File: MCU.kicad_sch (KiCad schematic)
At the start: 16 parts, among them J1 USB_C_Receptacle, J3 Conn_01x06, SW3 SW_Push, SW4 SW_Push, SW5 SW_Push, SW6 SW_Push, SW7 SW_Push, U11 ESDR0502NMUTBG, U3 NORA-B106-00B, U8 FAN5622SX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

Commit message: WIP changes
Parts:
- removed J1: USB_C_Receptacle, Connector_USB:USB_C_Receptacle_Amphenol_12401548E4-2A, symbol Connector:USB_C_Receptacle
- added J5: USB_C_Receptacle_USB2.0_16P, Connector_USB:USB_C_Receptacle_GCT_USB4105-xx-A_16P_TopMnt_Horizontal, symbol Connector:USB_C_Receptacle_USB2.0_16P
- SW3: footprint SKRPACE:SW_SKRPACE010_AAL -> Resistor_SMD:R_0805_2012Metric
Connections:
- net CC1: now also J5.A5 (CC1)
- net CC2: now also J5.B5 (CC2)
- net GND: now also J5.A1 (GND), J5.A12 (GND), J5.B1 (GND), J5.B12 (GND), J5.SH (SHIELD)
- net USBC_D+: now also J5.A6 (D+), J5.B6 (D+)
- net USBC_D-: now also J5.A7 (D-), J5.B7 (D-)
- net USB_RST: now also J5.A8 (SBU1), J5.B8 (SBU2)
- net VBUS_IN: now also J5.A4 (VBUS), J5.A9 (VBUS), J5.B4 (VBUS), J5.B9 (VBUS)
- no-connect marks 25 -> 17
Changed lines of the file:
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@@
 	)
 	(junction
-		(at 172.72 157.48)
+		(at 25.4 100.33)
 		(diameter 0)
 		(color 0 0 0 0)
 	)
 	(junction
-		(at 40.64 118.11)
+		(at 172.72 157.48)
 		(diameter 0)
 		(color 0 0 0 0)
@@
 	)
 	(junction
-		(at 25.4 128.27)
+		(at 40.64 90.17)
 		(diameter 0)
 		(color 0 0 0 0)
@@
 	)
 	(no_connect
-		(at 40.64 97.79)
-	)
-	(no_connect
 		(at 172.72 53.34)
 	)
@@
 	)
 	(no_connect
-		(at 40.64 95.25)
-	)
-	(no_connect
 		(at 116.84 60.96)
 	)
@@
 	)
 	(no_connect
-		(at 40.64 105.41)
-	)
-	(no_connect
 		(at 172.72 60.96)
 	)
@@
 	)
 	(no_connect
-		(at 40.64 102.87)
-	)
-	(no_connect
 		(at 172.72 45.72)
 	)
 	(no_connect
-		(at 40.64 110.49)
-	)
-	(no_connect
 		(at 116.84 91.44)
 	)
@@
 		(at 172.72 76.2)
 	)
-	(no_connect
-		(at 40.64 113.03)
-	)
-	(no_connect
-		(at 40.64 90.17)
-	)
-	(no_connect
-		(at 40.64 87.63)
-	)
 	(wire
 		(pts
@@
 	(wire
 		(pts
-			(xy 40.64 118.11) (xy 50.8 118.11)
+			(xy 40.64 90.17) (xy 50.8 90.17)
 		)
 		(stroke
@@
 	(wire
 		(pts
-			(xy 40.64 118.11) (xy 40.64 120.65)
+			(xy 40.64 90.17) (xy 40.64 92.71)
 		)
 		(stroke
@@
 	(wire
 		(pts
-			(xy 25.4 128.27) (xy 17.78 128.27)
+			(xy 25.4 100.33) (xy 17.78 100.33)
 		)
 		(stroke
@@
 	)
 	(label "USB_RST"
-		(at 50.8 118.11 180)
+		(at 50.8 90.17 180)
 		(effects
 			(font
@@
 			)
 		)
-		(property "Footprint" "SKRPACE:SW_SKRPACE010_AAL"
+		(property "Footprint" "Resistor_SMD:R_0805_2012Metric"
 			(at 104.14 25.4 0)
 			(hide yes)
@@
 	)
 	(symbol
+		(lib_id "Connector:USB_C_Receptacle_USB2.0_16P")
+		(at 25.4 77.47 0)
+		(unit 1)
+		(body_style 1)
+		(exclude_from_sim no)
+		(in_bom yes)
+		(on_board yes)
+		(in_pos_files yes)
+		(dnp no)
+		(fields_autoplaced yes)
+		(property "Reference" "J5"
+			(at 25.4 55.5455 0)
+			(show_name no)
+			(do_not_autoplace no)
+			(effects
+				(font
+					(size 1.27 1.27)
+				)
+			)
+		)
+		(property "Value" "USB_C_Receptacle_USB2.0_16P"
+			(at 25.4 57.9698 0)
+			(show_name no)
+			(do_not_autoplace no)
+			(effects
+				(font
+					(size 1.27 1.27)
+				)
+			)
+		)
+		(property "Footprint" "Connector_USB:USB_C_Receptacle_GCT_USB4105-xx-A_16P_TopMnt_Horizontal"
+			(at 29.21 77.47 0)
+			(hide yes)
+			(show_name no)
+			(do_not_autoplace no)
+			(effects
+				(font
+					(size 1.27 1.27)
+				)
+			)
+		)
+		(property "Datasheet" "https://www.usb.org/sites/default/files/documents/usb_type-c.zip"
+			(at 29.21 77.47 0)
+			(hide yes)
+			(show_name no)
+			(do_not_autoplace no)
+			(effects
+				(font
+					(size 1.27 1.27)
+				)
+			)
+		)
+		(property "Description" "USB 2.0-only 16P Type-C Receptacle connector"
+			(at 25.4 77.47 0)
+			(hide yes)
+			(show_name no)
+			(do_not_autoplace no)
+			(effects
+				(font
+					(size 1.27 1.27)
+				)
+			)
+		)
+		(pin "A9"
+		)
+		(pin "A7"
+		)
+		(pin "A8"
+		)
+		(pin "A5"
+		)
+		(pin "B5"
+		)
+		(pin "B12"
+		)
+		(pin "B4"
+		)
+		(pin "A1"
+		)
+		(pin "SH"
+		)
+		(pin "A4"
+		)
+		(pin "B7"
+		)
+		(pin "B6"
+		)
+		(pin "B9"
+		)
+		(pin "A6"
+		)
+		(pin "A12"
+		)
+		(pin "B1"
+		)
+		(pin "B8"
+		)
+		(instances
+			(project "Smart_Watch"
+				(path "/69095a4d-0a57-4fa3-aecb-1cfd89eedc11/bed567dd-6d09-419a-b99a-3e57c9439bd4/30bd5bb3-3a33-4afa-baf2-7512abedf580"
+					(reference "J5")
+					(unit 1)
+				)
+			)
+		)
+	)
+	(symbol
 		(lib_id "power:+3V0")
 		(at 241.3 66.04 0)
@@
 	(symbol
 		(lib_id "power:GND")
-		(at 25.4 128.27 0)
+		(at 25.4 100.33 0)
 		(unit 1)
 		(body_style 1)
@@
 		(fields_autoplaced yes)
 		(property "Reference" "#PWR065"
-			(at 25.4 134.62 0)
+			(at 25.4 106.68 0)
 			(hide yes)
 			(show_name no)
@@
 		)
 		(property "Value" "GND"
-			(at 25.4 132.4031 0)
+			(at 25.4 104.4631 0)
 			(show_name no)
 			(do_not_autoplace no)
@@
 		)
 		(property "Footprint" ""
-			(at 25.4 128.27 0)
+			(at 25.4 100.33 0)
 			(hide yes)
 			(show_name no)
@@
 		)
 		(property "Datasheet" ""
-			(at 25.4 128.27 0)
+			(at 25.4 100.33 0)
 			(hide yes)
 			(show_name no)
@@
 		)
 		(property "Description" "Power symbol creates a global label with name \"GND\" , ground"
-			(at 25.4 128.27 0)
+			(at 25.4 100.33 0)
 			(hide yes)
 			(show_name no)
@@
 				)
 			)
-		)
-	)
-	(symbol
-		(lib_id "Connector:USB_C_Receptacle")
-		(at 25.4 87.63 0)
-		(unit 1)
-		(body_style 1)
-		(exclude_from_sim no)
-		(in_bom yes)
-		(on_board yes)
-		(in_pos_files yes)
-		(dnp no)
-		(fields_autoplaced yes)
-		(property "Reference" "J1"
-			(at 25.4 55.5455 0)
-			(show_name no)
-			(do_not_autoplace no)
-			(effects
-				(font
-					(size 1.27 1.27)
-				)
-			)
-		)
-		(property "Value" "USB_C_Receptacle"
-			(at 25.4 57.9698 0)
-			(show_name no)
-			(do_not_autoplace no)
-			(effects
-				(font
-					(size 1.27 1.27)
-				)
-			)
-		)
-		(property "Footprint" "Connector_USB:USB_C_Receptacle_Amphenol_12401548E4-2A"
-			(at 29.21 87.63 0)
-			(hide yes)
-			(show_name no)
-			(do_not_autoplace no)
-			(effects
-				(font
-					(size 1.27 1.27)
-				)
-			)
-		)
-		(property "Datasheet" "https://www.usb.org/sites/default/files/documents/usb_type-c.zip"
-			(at 29.21 87.63 0)
-			(hide yes)
-			(show_name no)
-			(do_not_autoplace no)
-			(effects
-				(font
-					(size 1.27 1.27)
-				)
-			)
-		)
-		(property "Description" "USB Full-Featured Type-C Receptacle connector"
-			(at 25.4 87.63 0)
-			(hide yes)
-			(show_name no)
-			(do_not_autoplace no)
-			(effects
-				(font
-					(size 1.27 1.27)
-				)
-			)
-		)
-		(pin "B12"
-		)
-		(pin "A9"
-		)
-		(pin "B9"
-		)
-		(pin "S1"
-		)
-		(pin "A7"
-		)
-		(pin "A12"
-		)
-		(pin "A1"
-		)
-		(pin "B1"
-		)
-		(pin "A4"
-		)
-		(pin "B4"
-		)
-		(pin "B5"
-		)
-		(pin "A5"
-		)
-		(pin "A11"
-		)
-		(pin "B6"
-		)
-		(pin "B11"
-		)
-		(pin "B2"
-		)
-		(pin "A6"
-		)
-		(pin "A3"
-		)
-		(pin "A2"
-		)
-		(pin "B3"
-		)
-		(pin "A10"
-		)
-		(pin "A8"
-		)
-		(pin "B10"
-		)
-		(pin "B8"
-		)
-		(pin "B7"
-		)
-		(instances
-			(project "Smart_Watch"
-				(path "/69095a4d-0a57-4fa3-aecb-1cfd89eedc11/bed567dd-6d09-419a-b99a-3e57c9439bd4/30bd5bb3-3a33-4afa-baf2-7512abedf580"
-					(reference "J1")
-					(unit 1)
-					(variant
-						(name "No Trans")
-					)
-					(variant
-						(name "W Trans")
-					)
-				)
-			)

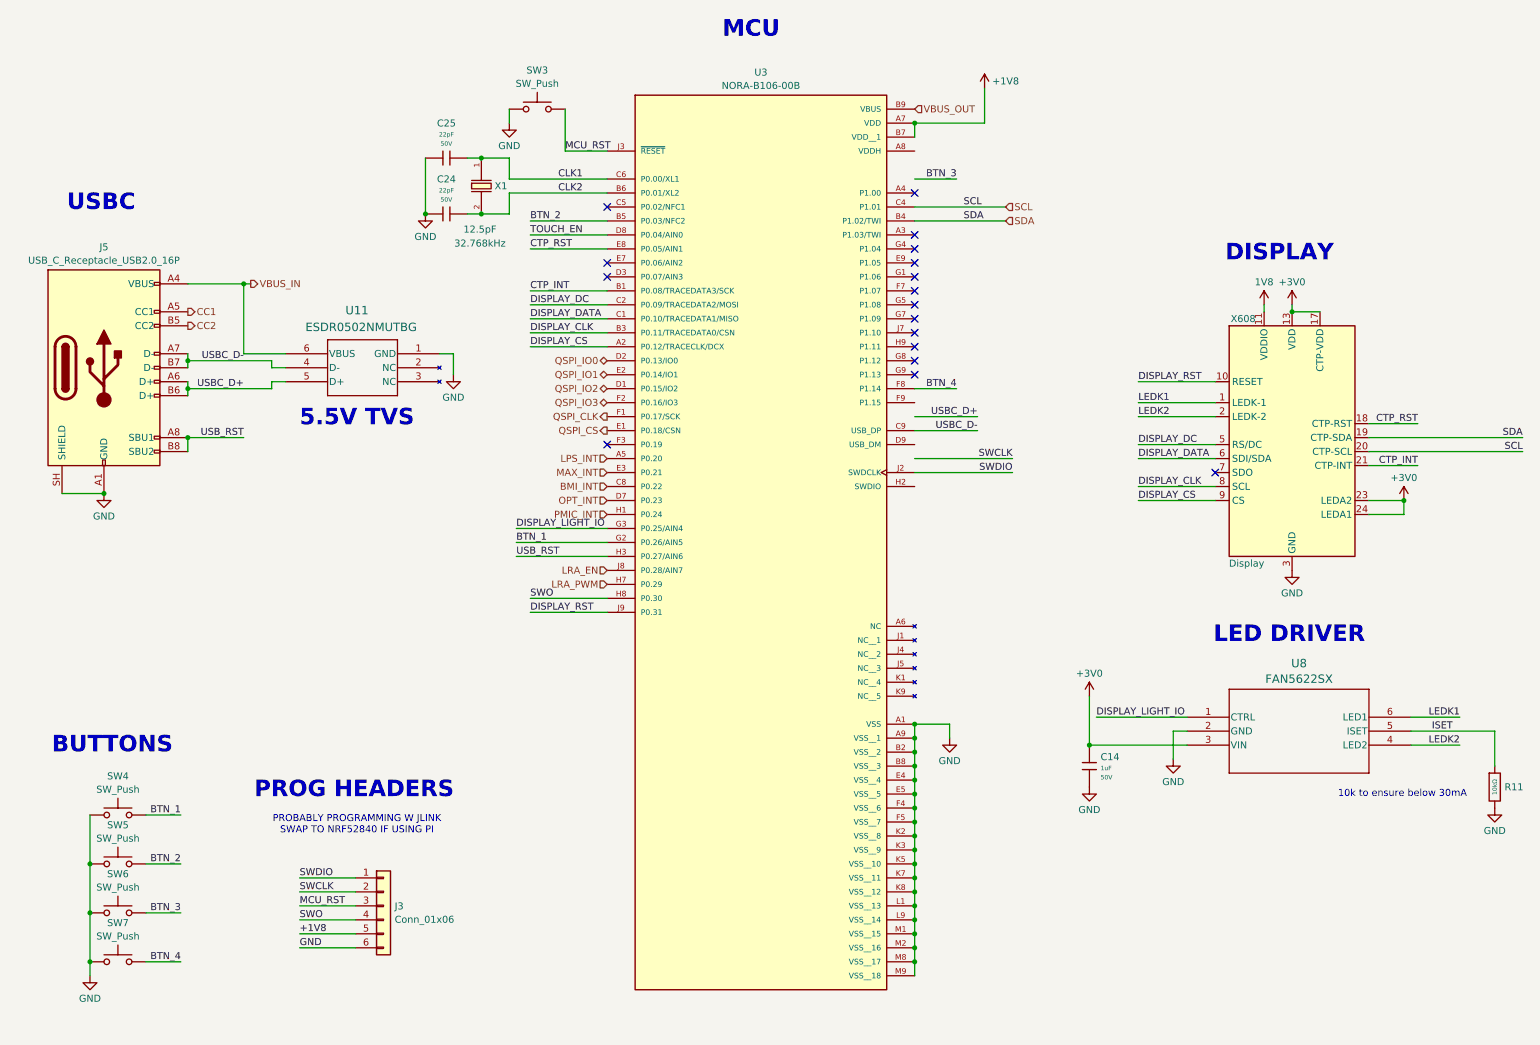
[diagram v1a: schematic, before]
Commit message: Update the last components and change a couple
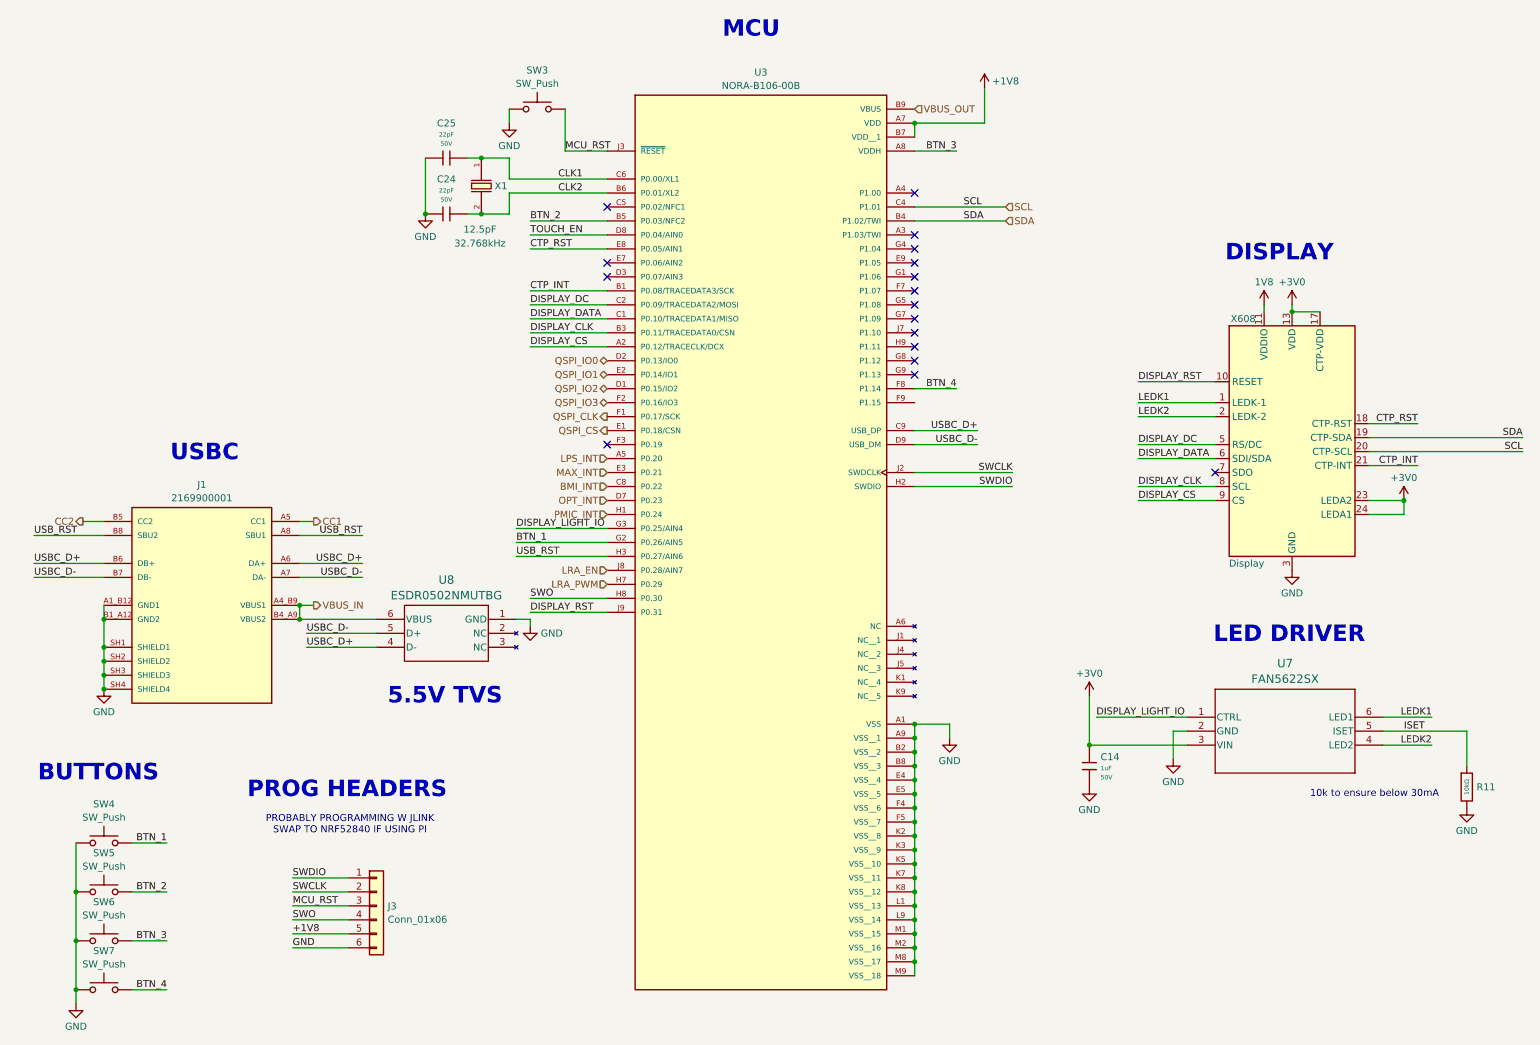
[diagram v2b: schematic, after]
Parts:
- removed J5: USB_C_Receptacle_USB2.0_16P, Connector_USB:USB_C_Receptacle_GCT_USB4105-xx-A_16P_TopMnt_Horizontal, symbol Connector:USB_C_Receptacle_USB2.0_16P
- removed U11: ESDR0502NMUTBG, ESD:UDFN6_517AA_ONS, symbol 2026-04-16_01-33-00:ESDR0502NMUTBG
- removed U8: FAN5622SX, FAN:SSOT6_3X1P7_ONS, symbol 2026-04-09_01-28-48:FAN5622SX
- added J1: 2169900001, Smart_Watch:MOLEX_2169900001, symbol Smart_Watch:2169900001
- added U7: FAN5622SX, Smart_Watch:SSOT6_3X1P7_ONS-L, symbol Smart_Watch:FAN5622SX
- added U8: ESDR0502NMUTBG, Smart_Watch:UDFN6_517AA_ONS-L, symbol Smart_Watch:ESDR0502NMUTBG
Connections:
- net +3V0: now also U7.3 (VIN)
- net BTN_3: now also U3.A8 (VDDH)
- net CC1: now also J1.A5 (CC1)
- net CC2: now also J1.B5 (CC2)
- net DISPLAY_LIGHT_IO: now also U7.1 (CTRL)
- net GND: now also J1.A1_B12 (GND1), J1.B1_A12 (GND2), J1.SH1 (SHIELD1), J1.SH2 (SHIELD2), J1.SH3 (SHIELD3), J1.SH4 (SHIELD4), U7.2 (GND), U8.1 (GND)
- net ISET: now also U7.5 (ISET)
- net LEDK1: now also U7.6 (LED1)
- net LEDK2: now also U7.4 (LED2)
- net SWCLK: now also U3.J2 (SWDCLK)
- net SWDIO: now also U3.H2 (SWDIO); no longer U3.J2 (SWDCLK)
- net USBC_D+: now also U3.C9 (USB_DP), J1.A6 (DA+), J1.B6 (DB+), U8.4 (D-)
- net USBC_D-: now also U3.D9 (USB_DM), J1.A7 (DA-), J1.B7 (DB-), U8.5 (D+); no longer U3.C9 (USB_DP)
- net USB_RST: now also J1.A8 (SBU1), J1.B8 (SBU2)
- net VBUS_IN: now also J1.A4_B9 (VBUS1), J1.B4_A9 (VBUS2), U8.6 (VBUS)
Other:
- moved on the sheet: J3, R11, SW4, SW5, SW6, SW7

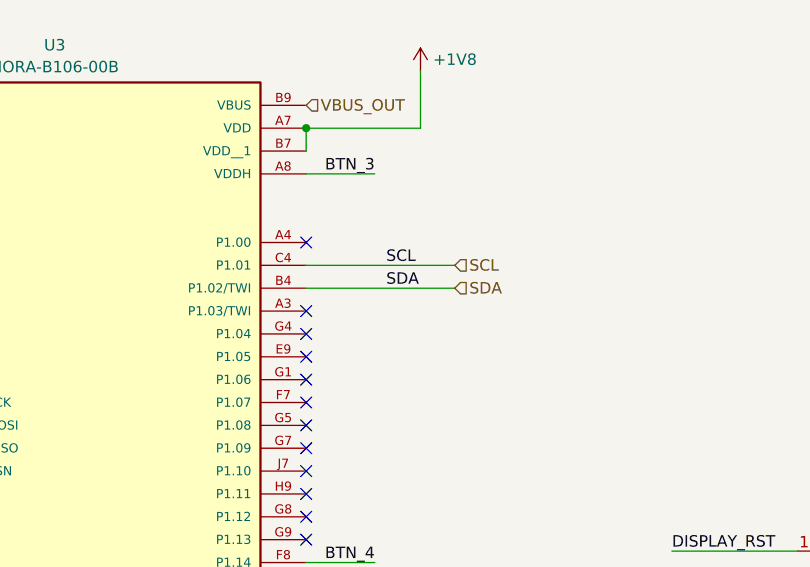
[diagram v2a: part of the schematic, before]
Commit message: Added Backpack Integration + Layout V1
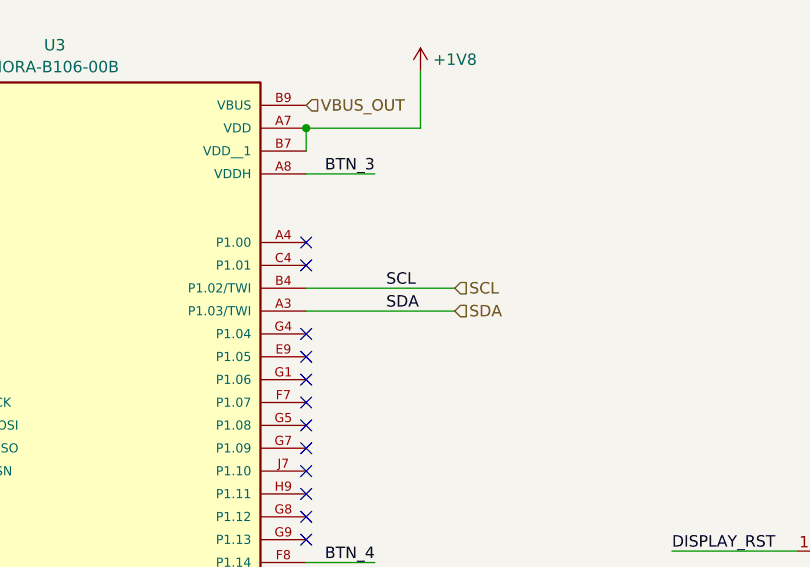
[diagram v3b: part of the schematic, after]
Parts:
- SW3: now left out of the parts list
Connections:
- net SCL: now also U3.B4 (P1.02/TWI); no longer U3.C4 (P1.01)
- net SDA: now also U3.A3 (P1.03/TWI); no longer U3.B4 (P1.02/TWI)

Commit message: Began Backpack Removal to Lower Profile
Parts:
- C14: Price 0.008USD -> (none)
- C24, C25: Price 0.007USD -> (none)
- R11: Price 0.004USD -> (none)
- X1: Price 0.182USD -> (none)

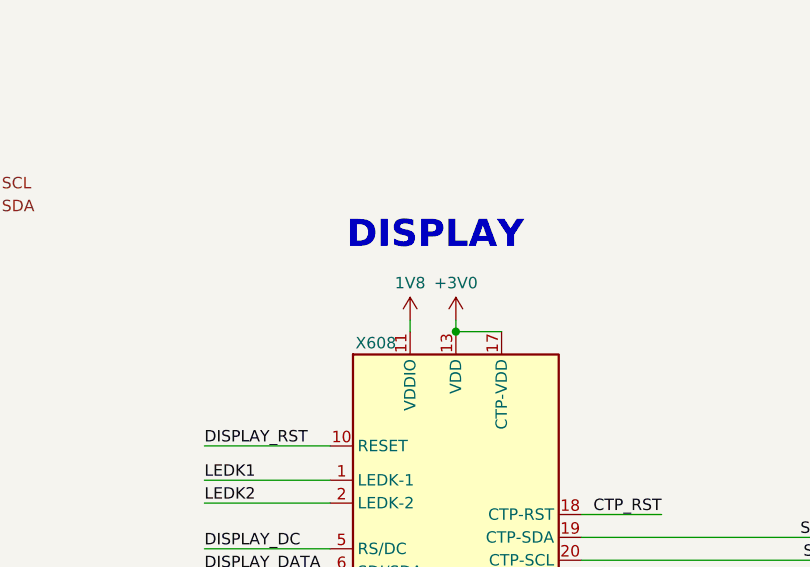
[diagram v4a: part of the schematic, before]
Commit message: Everything Moved to Front
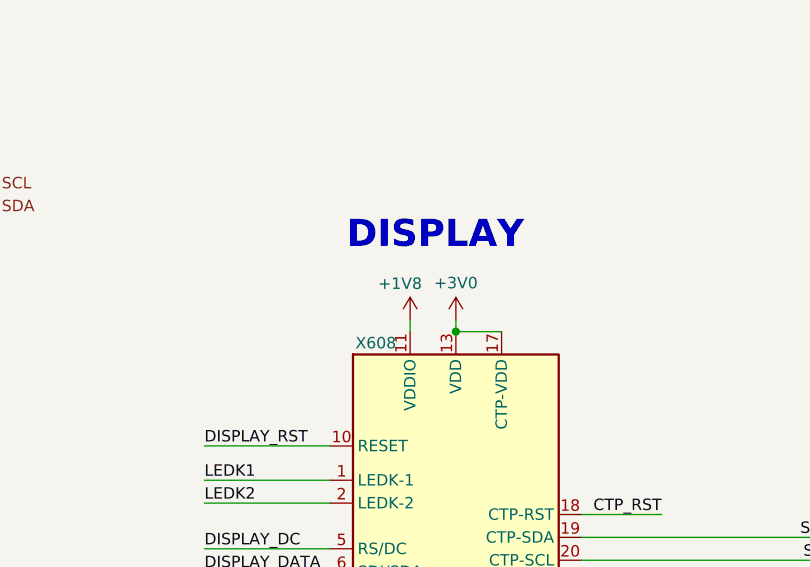
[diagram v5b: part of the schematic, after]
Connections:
- net 1V8 is gone; now on net +1V8: X608.11 (VDDIO), X608.12 (VDDIO)
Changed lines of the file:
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@@
 		(in_pos_files yes)
 		(dnp no)
-		(fields_autoplaced yes)
 		(property "Reference" "#PWR040"
 			(at 236.22 69.85 0)
@@
 			)
 		)
-		(property "Value" "1V8"
-			(at 236.22 61.9069 0)
+		(property "Value" "+1V8"
+			(at 232.664 61.976 0)
 			(show_name no)
 			(do_not_autoplace no)
@@
 					(size 1.27 1.27)
 				)
+				(justify right)
 			)
 		)
